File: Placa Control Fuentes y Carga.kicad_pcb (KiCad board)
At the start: 2 copper layers, 150 x 90 mm, 138 parts, among them J1 TBP01R1-508-02BE, J10 TBP01R1-508-03BE, J2 TBP01R1-508-02BE, J3 TBP01R1-508-02BE, J4 TBP01R1-508-02BE, J5 TBP01R1-508-02BE, J6 TBP01R1-508-02BE, J7 TBP01R1-508-02BE, J8 TBP01R1-508-02BE, J9 TBP01R1-508-02BE, Q1 IRF9540N, Q2 2N3904, Q3 BC558, Q4 BC558, Q5 IRF5305, Q6 BC337, Q7 BC327, U1 ACS724LLCTR-05AB-T, U2 Relay_Module_WB-083, U3 4N35, U4 LM2596S_Modulo_Regulable, U5 Arduino_Nano_ATmega328P, U6 ACS724LLCTR-05AB-T, U7 MAX485E, U8 MAX22445FAWE+, U9 RI3-0505S

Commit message: feat(pcb): placement inicial y netlist vinculada en placa 2 capas
- Placa 2 capas FR4 1.6 mm; contorno Edge.Cuts ~160 x 95 mm
- 142 footprints colocados (cara top); netlist asociada a pads
- Dominios de tierra en netlist: GND (principal) y GND_B (RS-485 aislado)
- Secciones ubicadas: entrada/OR-ing, LM2596, sensado ACS724, rele,
  RS-485 (MAX485E/MAX22445/RI3-0505S) y deteccion 220 VCA (4N35/GDT)

Pendiente (no incluido en este commit):
- Ruteo de senal y potencia
- Planos/zonas GND y GND_B (validar que NO se unan en cobre)
- Vias de costura y de retorno
- Barrera de fresado bajo U3 (4N35) para creepage 220 VCA
- Anchos de pista de potencia por IPC-2152
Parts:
- removed the RV1 at (333.7, 132.0)
- removed the RV2 at (333.7, 136.1)
- added C16: F102K43Y5RP6UK5R, Damian_PCB:CAP_F_11X5P_VIS, F.Cu at (177.5, 140.4)
- added D16: 1N4733A, Diode_THT:D_DO-41_SOD81_P10.16mm_Horizontal, F.Cu at (188.9, 77.7)
- added R24: B72214S0271K101, Damian_PCB:VARS_B72214S0271K101_TDK, F.Cu at (79.3, 78.8)
- added R25: B72214S0271K101, Damian_PCB:VARS_B72214S0271K101_TDK, F.Cu at (79.3, 62.6)
- added R26: 1M, Resistor_THT:R_Axial_DIN0207_L6.3mm_D2.5mm_P7.62mm_Horizontal, F.Cu at (181.9, 148.0)
- added TP26: TestPoint, TestPoint:TestPoint_THTPad_D2.5mm_Drill1.2mm, F.Cu at (188.8, 73.8)
- R3, R4: value 56K -> 56K 0.5W; footprint Resistor_THT:R_Axial_DIN0207_L6.3mm_D2.5mm_P7.62mm_Horizontal -> Resistor_THT:R_Axial_DIN0309_L9.0mm_D3.2mm_P12.70mm_Horizontal
- moved JP4 322.1 mm to (93.8, 84.2), turned to 90 degrees
- moved J10 320.5 mm to (99.3, 65.8)
- moved U3 317.0 mm to (102.2, 133.8)
- moved D10 314.3 mm to (116.9, -19.6)
- moved D13 314.0 mm to (94.1, 57.0), turned to 90 degrees
- moved D12 312.7 mm to (104.5, 80.3), turned to 90 degrees
- moved TP14 311.3 mm to (122.9, -24.9)
- moved F4 310.4 mm to (100.0, 84.0), turned to 90 degrees
- moved U8 309.0 mm to (98.3, 114.3), turned to 90 degrees
- moved J4 308.6 mm to (70.4, 69.9), turned to 90 degrees
- moved D15 306.6 mm to (96.3, 87.6), turned to 180 degrees
- moved TP17 305.4 mm to (87.5, 142.1)
- moved U7 305.3 mm to (99.8, 97.2), turned to 90 degrees
- moved TP18 304.9 mm to (92.8, 142.2)
- moved F3 303.0 mm to (107.7, 84.0), turned to 90 degrees
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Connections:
- D2 pad 1: Net-(D2-A) -> +12V
- D2 pad 2: +12V -> Net-(D2-A)
- D3 pad 1: Net-(D3-A) -> +12V
- D3 pad 2: +12V -> Net-(D3-A)
- D8 pad 1: Net-(D8-A) -> +12V
- D8 pad 2: +12V -> Net-(D8-A)
- J10 pad 1: Net-(GD1-A+) -> Net-(GD1-B-)
- J10 pad 3: Net-(GD1-B-) -> Net-(GD1-A+)
- U8 pad 5: unconnected-(U8-IN3-Pad5) -> GND
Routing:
- net Earth: track 0.00 -> 513.0 mm
- net Net-(J1-Pad1): track 0.00 -> 106.2 mm
- net Net-(U2-NC1): track 0.00 -> 78.1 mm
- net Net-(U2-C1): track 0.00 -> 62.6 mm
- net +5V_B: track 0.00 -> 52.1 mm, vias 0 -> 2
- net GND_B: track 0.00 -> 52.1 mm
- net Net-(U2-NC2): track 0.00 -> 43.4 mm
- net Net-(D14-K): track 0.00 -> 43.1 mm
- net Net-(D13-K): track 0.00 -> 42.0 mm
- net Net-(D1-K): track 0.00 -> 26.5 mm
- net Net-(D1-A): track 0.00 -> 18.7 mm
- net F220_IN: track 0.00 -> 16.2 mm
- net Net-(U7-DI): track 0.00 -> 15.4 mm, vias 0 -> 1
- net Net-(GD1-A+): track 0.00 -> 14.0 mm
- net Net-(U7-DE): track 0.00 -> 14.0 mm, vias 0 -> 1
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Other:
- board size 150 x 90 mm -> 160 x 95 mm

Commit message: feat(pcb): ruteo parcial + planos GND/+12V y keepouts de aislamiento
Estado actual:
- Placa 2 capas FR4 1.6 mm, contorno ~160 x 95 mm, 141 footprints
- Ruteo parcial: 400 segmentos (138 F.Cu / 262 B.Cu) + 6 vias
- Planos rellenados (locked): GND x4 (masa1-4, F.Cu/B.Cu, prio 1-3)
  y +12V (12V_1, B.Cu)
- 9 keepouts en F.Cu para barreras de aislamiento
- Netlist con GND y GND_B asignada a pads

Pendiente para cierre:
- Completar ruteo restante y dejar ratsnest en cero
- Dibujar el retorno/plano de GND_B (dominio RS-485 aislado): hoy NO
  existe zona de cobre para GND_B
- Verificar separacion fisica GND vs GND_B (sin solape ni via cruzada)
- Vias de costura en planos GND (paso 2.5-4 mm); hoy solo 6 vias
- Ranura de fresado bajo U3 (4N35) y creepage 220 VCA (faltan datos:
  clase de aislamiento, recubrimiento, grado de polucion)
- Validar anchos de potencia vs IPC-2152 (OR-ing, LM2596, rele, ACS724)
  con corrientes reales
- Confirmar stackup/peso de cobre (1 oz?), DRC limpio, TVS/desacoplos
  al ras del pin y serigrafia.
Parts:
- removed the F2 at (186.6, 64.5)
- moved C3 99.0 mm to (261.3, 118.8)
- moved C4 99.0 mm to (235.9, 117.5)
- moved U5 99.0 mm to (241.3, 87.8)
- moved C12 24.9 mm to (105.2, 110.1), turned to 90 degrees
- moved TP8 24.8 mm to (93.7, 124.5)
- moved C13 24.5 mm to (148.4, 130.6), turned to 90 degrees
- moved TP9 21.2 mm to (97.8, 124.5)
- moved TP10 18.6 mm to (101.9, 124.5)
- moved TP1 5.08 mm to (129.8, 135.2)
- moved TP4 4.74 mm to (116.2, 144.0)
- moved JP3 3.93 mm to (203.0, 90.8), turned to 180 degrees
- moved TP26 2.21 mm to (191.0, 73.6)
- moved D16 2.20 mm to (190.9, 76.8)
- moved TP12 0.95 mm to (183.5, 100.4)
- moved TP2 0.95 mm to (140.1, 131.1)
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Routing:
- net GND: track 3.59 -> 315.5 mm
- net +12V: track 0.00 -> 70.1 mm, vias 0 -> 3
- net +5V: track 0.00 -> 64.8 mm
- net Net-(D3-A): track 0.00 -> 56.3 mm
- net Net-(D2-A): track 0.00 -> 56.0 mm
- net GND_B: track 52.1 -> 92.4 mm
- net +5V_B: track 52.1 -> 80.9 mm, vias 2 -> 1
- net Net-(F2-Pad2): track 0.00 -> 22.6 mm
- net ADC2: track 0.00 -> 15.5 mm
- net ADC1: track 0.00 -> 15.2 mm
- net Net-(F5-Pad1): track 0.00 -> 14.3 mm
- net Net-(F6-Pad1): track 0.00 -> 13.5 mm
- net Net-(JP3-B): track 0.00 -> 12.8 mm
- net ADC5: track 0.00 -> 12.0 mm
- net DE/RE: track 0.00 -> 7.02 mm
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- added copper zone on B.Cu, net +12V
- added copper zone on B.Cu, net GND
- added copper zone on F.Cu, net GND
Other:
- outline, holes or cut-outs redrawn

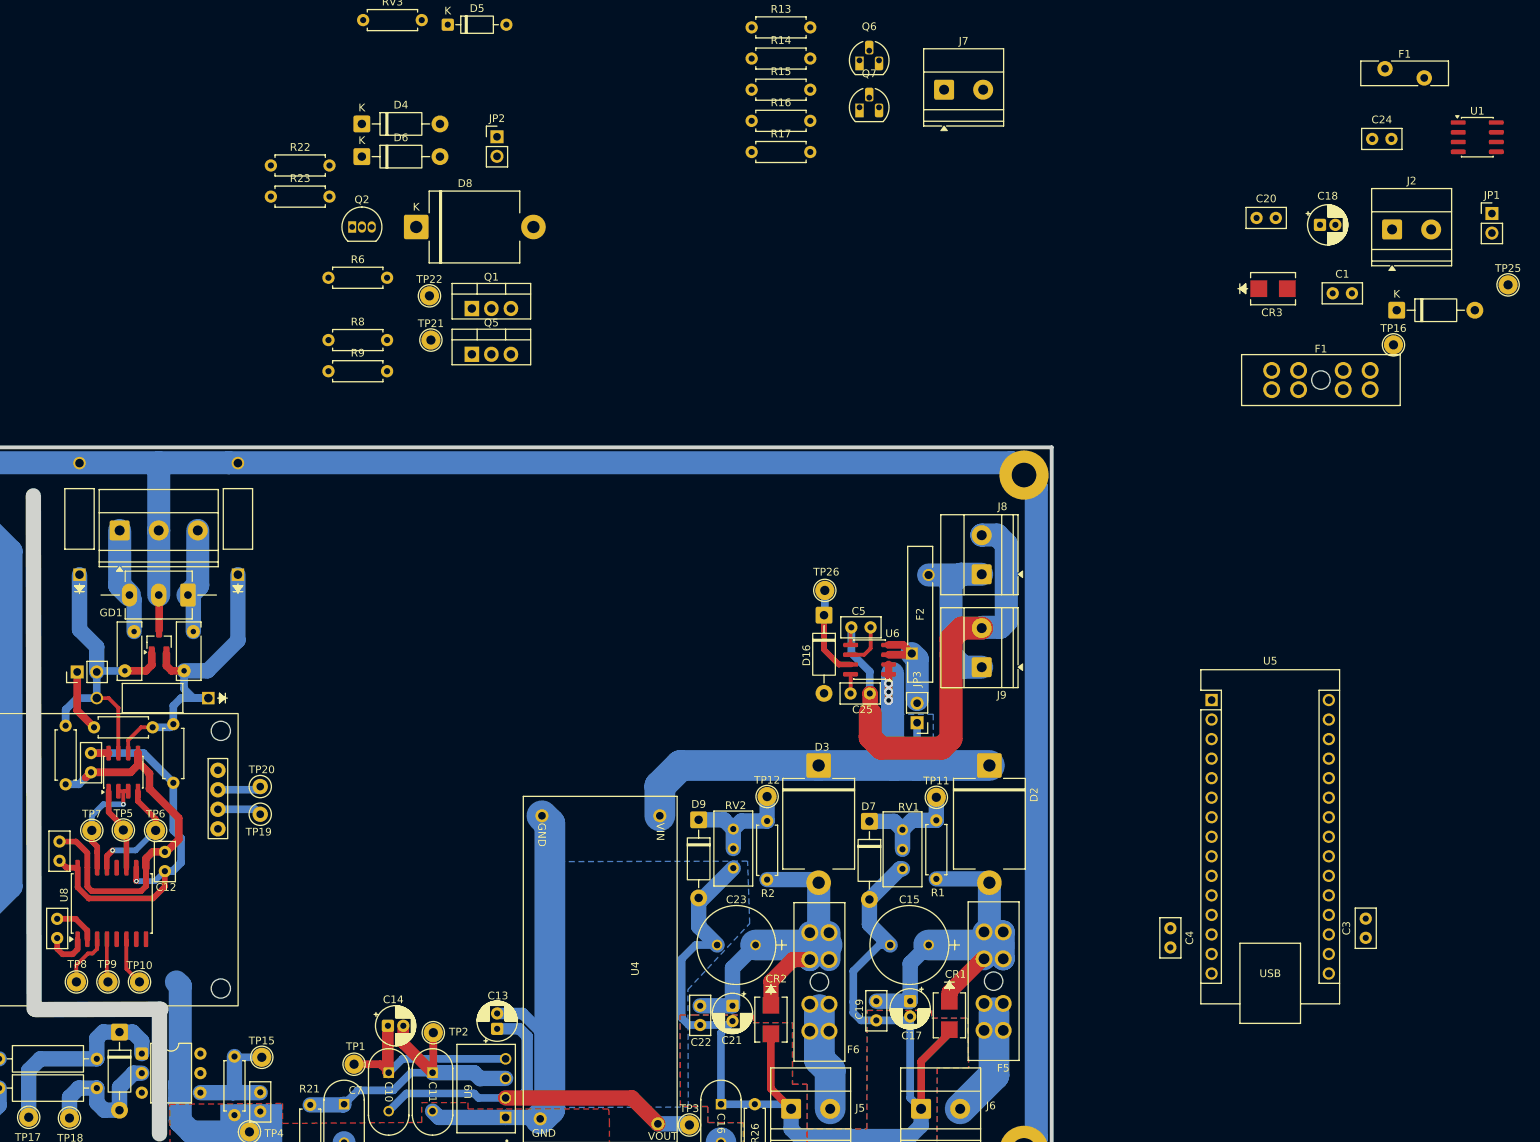
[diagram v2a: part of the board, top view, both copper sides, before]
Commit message: En relación a la versión anterior, comenzamos a acomodar las conexiones de batería.
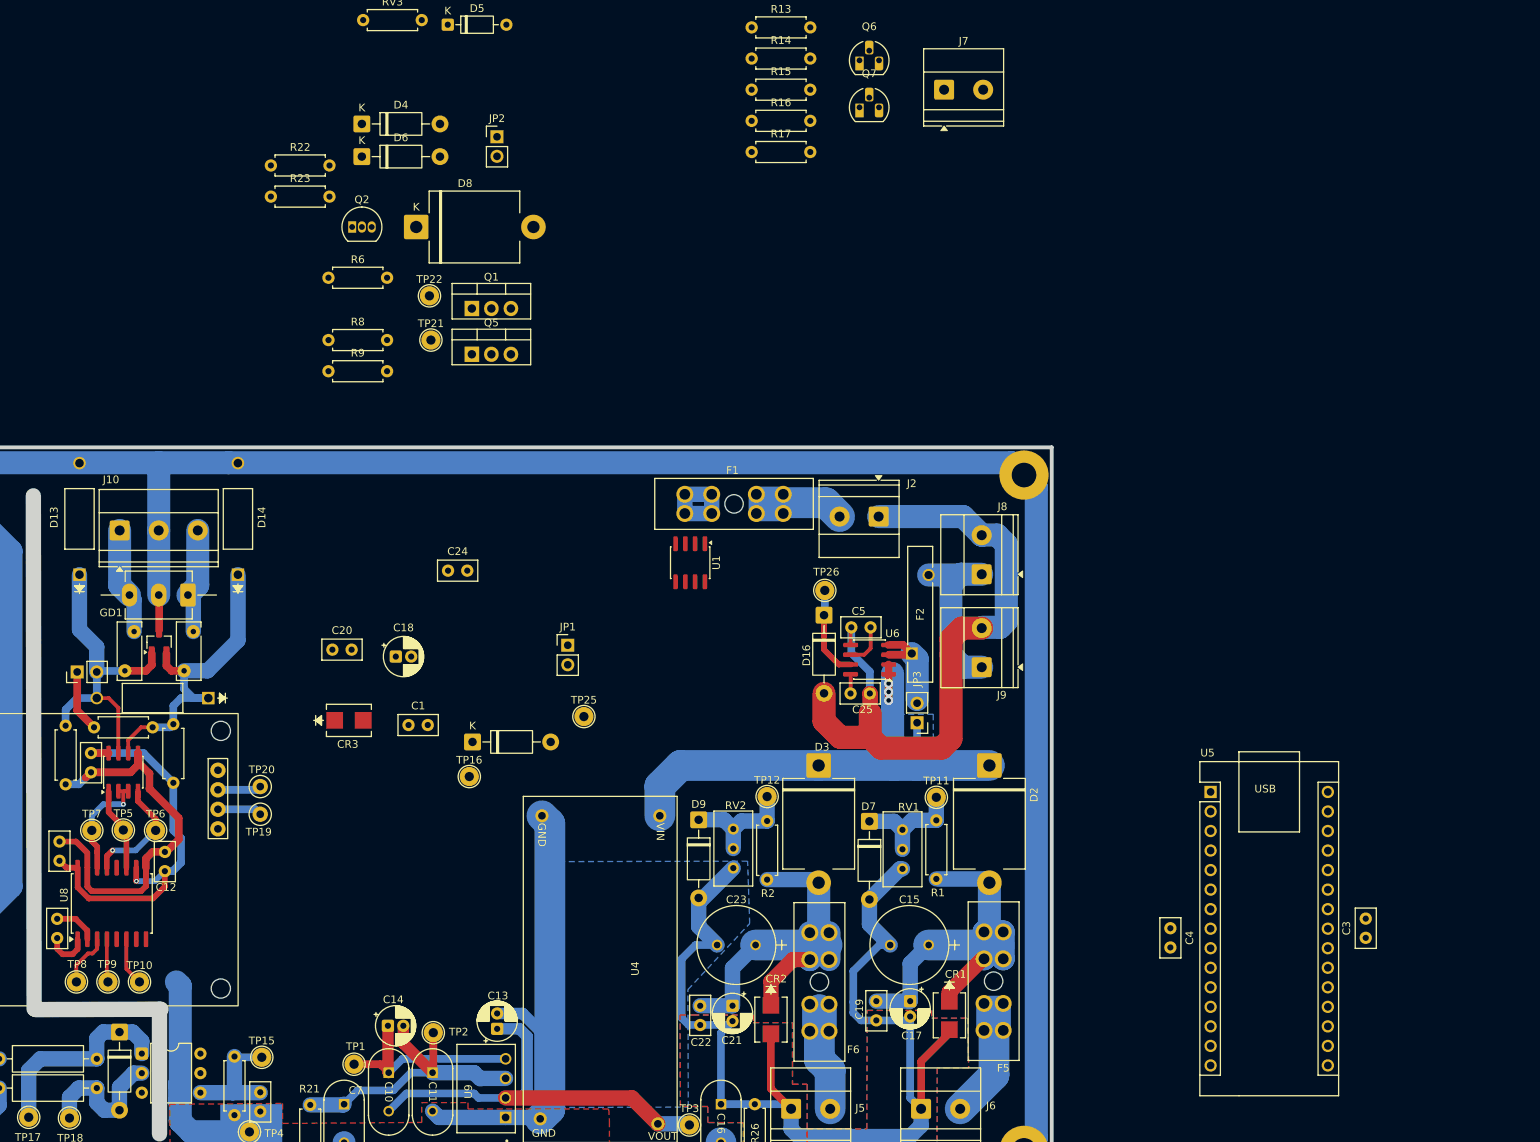
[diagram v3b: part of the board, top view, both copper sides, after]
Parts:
- removed the F1 at (263.8, 5.77)
- moved C1 132.6 mm to (136.9, 91.1)
- moved C24 132.6 mm to (142.0, 71.0)
- moved D11 132.6 mm to (145.2, 93.3)
- moved C18 132.6 mm to (135.2, 82.2)
- moved CR3 132.6 mm to (129.1, 90.5)
- moved JP1 132.6 mm to (157.6, 80.7)
- moved TP16 132.6 mm to (144.8, 97.8)
- moved TP25 132.6 mm to (159.7, 90.0)
- moved C20 132.6 mm to (127.0, 81.3)
- moved U1 116.3 mm to (173.5, 70.0), turned to -90 degrees
- moved J2 76.5 mm to (198.0, 64.0), turned to 180 degrees
- moved F1 66.2 mm to (185.6, 63.6), turned to 180 degrees
- moved U5 12.0 mm to (241.2, 99.8)
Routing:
- net GND: track 315.5 -> 340.4 mm
- net Net-(F1-Pad1): track 0.00 -> 22.4 mm
- net Net-(JP1-A): track 0.00 -> 12.0 mm
- net Net-(F6-Pad1): track 13.5 -> 25.5 mm
- net Net-(F5-Pad1): track 14.3 -> 23.8 mm
- net Net-(D2-A): track 56.0 -> 59.5 mm

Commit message: feat(pcb): ruteo casi completo + planos GND/+5V/+12V y earth ancho
== Avances mas notables ==
- Ruteo: 682 segmentos (242 F.Cu / 440 B.Cu) + 19 vias
- 57/76 nets ruteadas; solo faltan 2 senales reales: ADC0 y PWM
  (el resto de "unconnected" son pads NC de U5/U2/U3/U8)
- Planos rellenados (locked): GND x4 (masa1-4, F.Cu+B.Cu),
  +5V (cincoV1, F.Cu) y +12V (B.Cu)
- Dominio aislado RS-485 cableado: GND_B (36 seg) y +5V_B (25 seg)
- Earth de proteccion ruteado ancho (3-5 mm, 22 seg)
- 9 keepouts de aislamiento en F.Cu
- Anchos de potencia generosos (+12V/GND/Earth hasta 3-4 mm)

== Pendiente para finalizar ==
- Rutear ADC0 y PWM; dejar ratsnest en cero
- GND_B/+5V_B estan solo como pistas: definir isla/retorno de GND_B
  (hoy NO existe zona de cobre para el retorno aislado)
- Verificar separacion GND vs GND_B (sin cruces ni acoplamiento)
- Reforzar via stitching en los planos GND (solo 19 vias)
- Barrera 220 VCA: confirmar ranura de fresado bajo U3 (4N35) y fijar
  creepage/clearance (faltan: clase de aislamiento, recubrimiento,
  grado de polucion)
- Validar anchos vs IPC-2152 con corrientes reales
- Confirmar stackup/peso de cobre (1 oz?), DRC limpio y serigrafia.
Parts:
- removed the RV3 at (131.0, -0.55)
- moved R11 130.7 mm to (149.8, 117.6), turned to 90 degrees
- moved C3 127.3 mm to (134.1, 115.1), turned to -90 degrees
- moved Q3 123.7 mm to (143.0, 111.9)
- moved D10 121.5 mm to (149.8, 97.4), turned to -90 degrees
- moved TP14 121.0 mm to (149.0, 93.2)
- moved RV3 116.9 mm to (158.9, 97.4)
- moved R7 115.9 mm to (144.2, 107.6), turned to 90 degrees
- moved R5 114.6 mm to (159.6, 93.3), turned to 180 degrees
- moved TP24 113.6 mm to (141.0, 107.6)
- moved U5 106.4 mm to (136.7, 120.2), turned to 180 degrees
- moved C4 105.2 mm to (133.8, 92.2), turned to 90 degrees
- moved R12 103.5 mm to (168.6, 88.0), turned to -90 degrees
- moved D5 100.1 mm to (146.9, 100.0), turned to -90 degrees
- moved TP23 99.4 mm to (159.0, 87.3)
- moved Q4 94.2 mm to (164.5, 87.0), turned to 180 degrees
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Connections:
- J7 pad 1: Net-(Q7-C) -> GND
- J7 pad 2: GND -> Net-(Q7-C)
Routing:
- net GND: track 340.4 -> 584.9 mm
- net +5V: track 64.8 -> 218.7 mm, vias 0 -> 7
- net Net-(D4-K): track 0.00 -> 62.1 mm
- net +12V: track 70.1 -> 126.6 mm, vias 3 -> 9
- net Net-(Q7-B): track 0.00 -> 39.6 mm
- net Net-(JP1-A): track 12.0 -> 42.0 mm
- net ADC5: track 12.0 -> 38.4 mm
- net Net-(Q2-C): track 0.00 -> 25.8 mm
- net ADC4: track 0.00 -> 19.3 mm
- net Net-(D8-A): track 0.00 -> 17.8 mm
- net Net-(Q3-C): track 0.00 -> 17.2 mm
- net Net-(D6-K): track 0.00 -> 14.7 mm
- net ADC3: track 0.00 -> 14.6 mm
- net Net-(Q2-B): track 0.00 -> 11.4 mm
- net Net-(Q7-C): track 0.00 -> 10.8 mm
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- added copper zone on F.Cu, net +5V
